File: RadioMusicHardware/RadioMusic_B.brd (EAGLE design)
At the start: 106 x 19.7 mm, 33 parts, among them IC1 TL072P, IC2 TL072P, IC3 7805L, U1 TEENSY_3.1_TW

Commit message: Back board reworking
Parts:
- removed IC1, IC2: TL072P, TomW:DIL08
- removed R6: (no value), bourns:3362P
- added IC4: TL074, linear:DIL14
- added OUTPUT: (no value), bourns:3362P
- D1, D2, D3, D4: value BAT81 -> (none)
- JP1: value M11LOCK -> M11PTH; device SparkFun-Connectors:1X11_LOCK -> SparkFun-Connectors:1X11
- JP3: device SparkFun-Connectors:1X07_LOCK -> SparkFun-Connectors:1X07
- moved C8 34.0 mm to (72.4, 9.53)
- moved JP1 22.9 mm to (82.5, 17.1), turned to 180 degrees
- moved IC3 20.1 mm to (26.0, 6.99), turned to 270 degrees
- moved C5 15.5 mm to (50.8, 8.76)
- moved R7 11.4 mm to (82.5, 8.89)
- moved D3 11.2 mm to (21.4, 8.31), turned to 270 degrees
- moved D4 11.0 mm to (19.1, 8.31), turned to 90 degrees
- moved C1 10.9 mm to (40.0, 1.27), turned to 0 degrees
- moved R2 10.2 mm to (17.1, 9.53)
- moved R5 8.47 mm to (49.5, 1.27), turned to 0 degrees
- moved C4 6.38 mm to (45.7, 8.89), turned to 270 degrees
- moved JP3 4.49 mm to (57.1, 1.27)
- moved C2 3.86 mm to (38.1, 8.89)
- moved C6 3.17 mm to (87.0, 6.35), turned to 180 degrees
- moved D2 2.84 mm to (8.89, 9.53), turned to 90 degrees
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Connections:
- new net N$3: IC4.6, IC4.7, R1.2
- net +12V: now also C5.2, IC4.4; no longer C5.1, IC1.8, IC2.8
- net -12V: now also C8.2, IC4.11; no longer C8.1, IC1.4, IC2.4
- net AUDIO_OUT: now also IC4.1, OUTPUT.2, OUTPUT.3; no longer IC2.1, R6.2, R6.3
- net CHANNEL_CV: now also IC4.5; no longer IC1.3
- net DGND: no longer C5.2, C8.2
- net GND: now also C5.1, C8.1, JP1.1, R7.2; no longer JP1.11, R7.1
- net LED1: now also JP1.2; no longer JP1.1
- net LED2: now also JP1.3; no longer JP1.2
- net LED3: now also JP1.4; no longer JP1.3
- net LED4: now also JP1.5; no longer JP1.4
- net LED_RESET: now also JP1.10; no longer JP1.9
- net MISO: now also JP1.11; no longer JP1.10
- net MOSI: now also JP1.6; no longer JP1.5
- net N$1: now also IC4.8, IC4.9, R2.2; no longer IC1.6, IC1.7, R2.1
- net N$10: now also R3.2; no longer R3.1
- net N$2: now also IC4.12, R4.2; no longer IC2.5, R4.1
- net N$4: now also R3.1, R4.1; no longer R3.2, R4.2
- net N$5: now also C3.1, IC4.13, IC4.14; no longer C3.2, IC2.6, IC2.7
- net N$6: now also C3.2, IC4.3; no longer C3.1, IC2.3
- net N$7: now also IC4.2, OUTPUT.1, R7.1; no longer IC2.2, R6.1, R7.2
- net PIN20/A6: now also R2.1; no longer R2.2
- net PIN22/A8: no longer IC1.1, IC1.2, R1.2
- net RESET_CV: now also JP1.8; no longer JP1.7
- net RESET_SW: now also JP1.7; no longer JP1.6
- net SS: now also JP1.9; no longer JP1.8
- net TIME_CV: now also IC4.10; no longer IC1.5
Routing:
- net +12V: track 0.00 -> 71.4 mm
- net LED1: track 0.00 -> 71.0 mm
- net LED2: track 0.00 -> 64.0 mm
- net LED3: track 0.00 -> 59.0 mm
- net LED4: track 0.00 -> 54.0 mm
- net N$1: track 0.00 -> 53.7 mm
- net MOSI: track 0.00 -> 48.8 mm
- net RESET_SW: track 0.00 -> 44.3 mm
- net RESET_CV: track 0.00 -> 38.6 mm
- net SS: track 0.00 -> 34.1 mm
- net -12V: track 0.00 -> 32.7 mm
- net +5V: track 0.00 -> 29.6 mm
- net LED_RESET: track 0.00 -> 28.7 mm
- net MISO: track 0.00 -> 22.2 mm
- net -12V_INLET: track 0.00 -> 17.7 mm
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- added copper zone on layer 16, net DGND
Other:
- board size 106 x 19.7 mm -> 107 x 19.5 mm

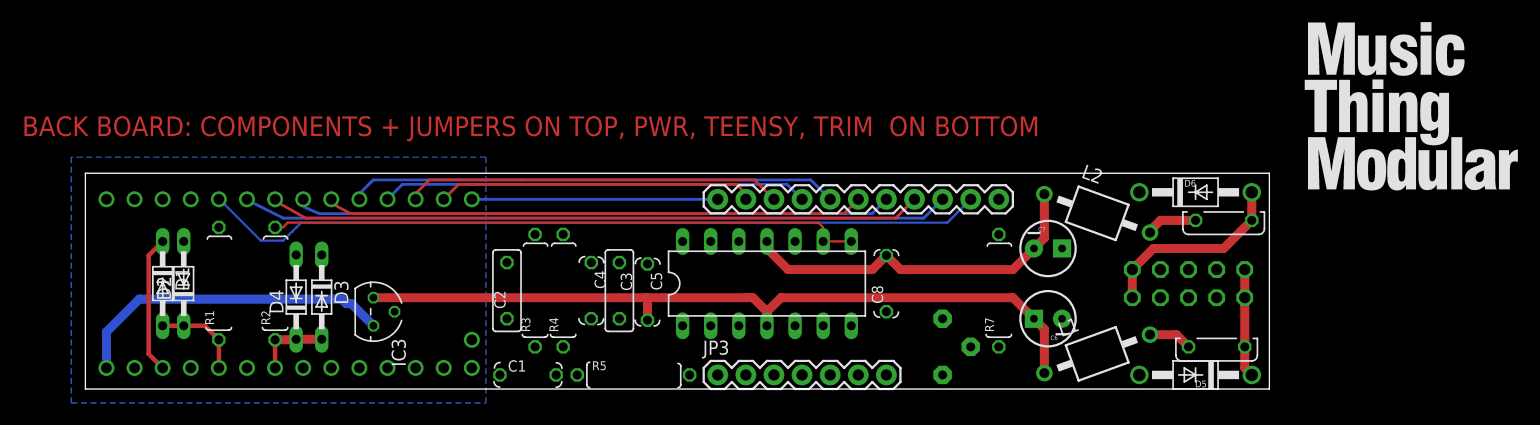
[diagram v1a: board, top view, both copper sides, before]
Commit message: Routed boards for checking
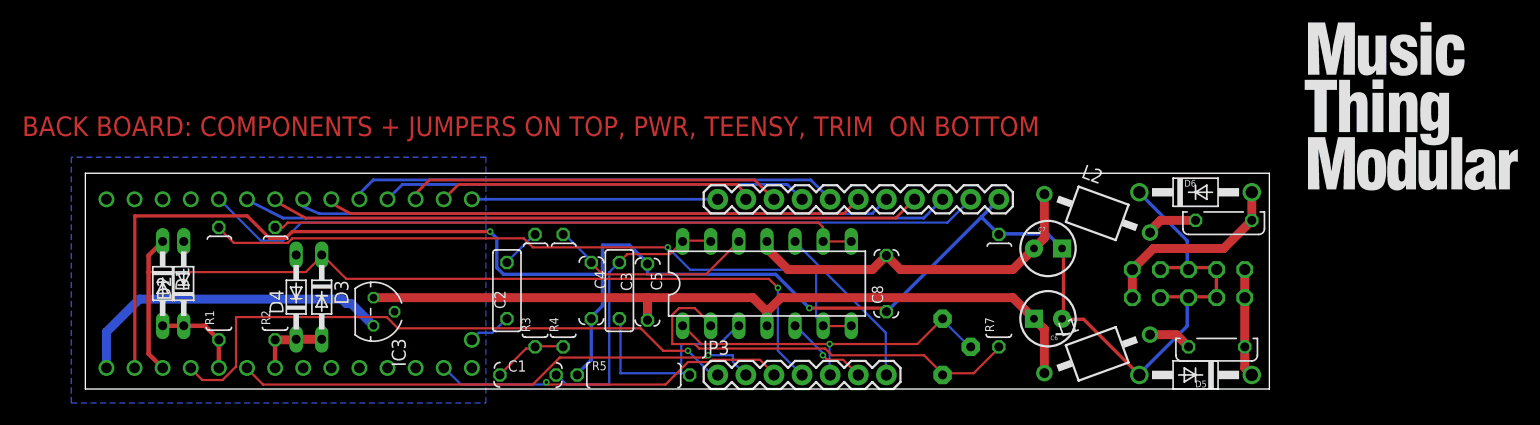
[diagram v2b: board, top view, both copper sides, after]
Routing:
- net GND: track 0.00 -> 170.9 mm, vias 0 -> 2
- net +3.3V: track 12.5 -> 80.0 mm, vias 0 -> 1
- net N$3: track 0.00 -> 63.8 mm, vias 0 -> 1
- net CHANNEL_POT: track 0.00 -> 55.3 mm, vias 0 -> 1
- net TIME_POT: track 0.00 -> 47.9 mm, vias 0 -> 1
- net N$7: track 0.00 -> 38.9 mm
- net SCLK: track 0.00 -> 32.3 mm, vias 0 -> 1
- net AUDIO_OUT: track 0.00 -> 31.6 mm, vias 0 -> 1
- net N$5: track 0.00 -> 25.7 mm
- net N$6: track 0.00 -> 19.8 mm
- net N$2: track 0.00 -> 18.8 mm
- net TIME_CV: track 0.00 -> 15.5 mm
- net CHANNEL_CV: track 0.00 -> 7.67 mm, vias 0 -> 1
- net N$4: track 0.00 -> 6.93 mm
- net DAC: track 0.00 -> 3.96 mm
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
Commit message: Artwork on panels, notes on PCBs
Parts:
- moved U$2 38.2 mm to (76.8, 0.15), flipped to the bottom, turned to 90 degrees
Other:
- board text added: "<-Set output volume"
- board text added: "Inspired by: John Cage Don Buchla Stockhausen Nicholas Collins Max Neuhaus, Akin Fernandez UbuWeb Resonance FM Thanks to: Paul Stoffregen, Steven Thonk The Muff Wigglers"
- board text added: "RadioMusic Back PCB Rev 1 Designed in Herne Hill, London by Tom Whitwell October 2014 CC-BY-SA musicthing.co.uk"
- board text added: "TEENSY 3.1"
- board text added: "USB this end"
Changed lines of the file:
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@@
 <grid distance="16" unitdist="mil" unit="mil" style="lines" multiple="1" display="yes" altdistance="8" altunitdist="mil" altunit="mil"/>
 <layers>
-<layer number="1" name="Top" color="4" fill="1" visible="yes" active="yes"/>
+<layer number="1" name="Top" color="4" fill="1" visible="no" active="yes"/>
 <layer number="2" name="Route2" color="1" fill="3" visible="no" active="yes"/>
 <layer number="3" name="Route3" color="4" fill="3" visible="no" active="no"/>
 <layer number="14" name="Route14" color="1" fill="6" visible="no" active="no"/>
 <layer number="15" name="Route15" color="4" fill="6" visible="no" active="yes"/>
-<layer number="16" name="Bottom" color="1" fill="1" visible="yes" active="yes"/>
+<layer number="16" name="Bottom" color="1" fill="1" visible="no" active="yes"/>
 <layer number="17" name="Pads" color="2" fill="1" visible="yes" active="yes"/>
 <layer number="18" name="Vias" color="2" fill="1" visible="yes" active="yes"/>
-<layer number="19" name="Unrouted" color="6" fill="1" visible="yes" active="yes"/>
+<layer number="19" name="Unrouted" color="6" fill="1" visible="no" active="yes"/>
 <layer number="20" name="Dimension" color="15" fill="1" visible="yes" active="yes"/>
 <layer number="21" name="tPlace" color="7" fill="1" visible="yes" active="yes"/>
@@
 <layer number="24" name="bOrigins" color="15" fill="1" visible="yes" active="yes"/>
 <layer number="25" name="tNames" color="7" fill="1" visible="no" active="yes"/>
-<layer number="26" name="bNames" color="7" fill="1" visible="no" active="yes"/>
+<layer number="26" name="bNames" color="7" fill="1" visible="yes" active="yes"/>
 <layer number="27" name="tValues" color="7" fill="1" visible="no" active="yes"/>
-<layer number="28" name="bValues" color="7" fill="1" visible="no" active="yes"/>
+<layer number="28" name="bValues" color="7" fill="1" visible="yes" active="yes"/>
 <layer number="29" name="tStop" color="7" fill="3" visible="no" active="yes"/>
 <layer number="30" name="bStop" color="7" fill="6" visible="no" active="yes"/>
@@
 </text>
 <wire x1="53.5" y1="-10" x2="53.5" y2="30" width="0.1" layer="51"/>
-<wire x1="53.5" y1="-10" x2="53.5" y2="30" width="0.1" layer="51"/>
+<text x="71.12" y="7.3152" size="0.762" layer="22" rot="MR0">RadioMusic Back PCB  Rev 1
+Designed in Herne Hill, London by Tom Whitwell
+October 2014 CC-BY-SA
+musicthing.co.uk</text>
+<text x="73.5584" y="3.2512" size="1.016" layer="22" rot="MR0">&lt;-Set output volume</text>
+<text x="23.5712" y="7.7216" size="2.286" layer="22" rot="MR0">TEENSY 3.1</text>
+<text x="3.2512" y="13.8176" size="1.016" layer="22" rot="SMR270">USB this end</text>
+<text x="35.7632" y="15.4432" size="0.508" layer="22" rot="MR0" align="top-left">Inspired by:
+John Cage
+Don Buchla
+Stockhausen
+Nicholas Collins
+Max Neuhaus,
+Akin Fernandez
+UbuWeb
+Resonance FM
+Thanks to:
+Paul Stoffregen,
+Steven Thonk
+The Muff Wigglers</text>
 </plain>
 <attributes>
@@
 <attribute name="VALUE" x="104.14" y="15.24" size="0.6096" layer="27" ratio="10" rot="R180"/>
 </element>
-<element name="U$2" library="TW_logos" package="MTM_2CM_SCREEN_200DPI" value="" x="110.49" y="18.034"/>
-<element name="U1" library="TomW" package="TEENSY_3.1_TW" value="TEENSY_3.1_TW" x="18.415" y="9.525" rot="MR270"/>
+<element name="U$2" library="TW_logos" package="MTM_2CM_SCREEN_200DPI" value="" x="76.7588" y="0.1524" rot="MR90"/>
+<element name="U1" library="TomW" package="TEENSY_3.1_TW" value="TEENSY_3.1_TW" x="18.415" y="9.525" smashed="yes" rot="MR270"/>
 <element name="IC3" library="gm-regulators" package="TO92" value="7805L" x="26.035" y="6.985" rot="R270"/>
 <element name="D1" library="diode" package="DO34-7" value="" x="6.985" y="9.525" rot="R270"/>
@@
 </element>
 <element name="OUTPUT" library="bourns" package="3362P" value="" x="77.47" y="3.81" smashed="yes" rot="MR90">
-<attribute name="NAME" x="81.407" y="0.508" size="1.27" layer="26" ratio="10" rot="MR90"/>
 <attribute name="VALUE" x="72.263" y="0.5334" size="1.27" layer="28" ratio="10" rot="MR90"/>
 </element>

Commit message: PCB cosmetic changes
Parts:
- added U$1: (no value), TW_logos:MTM_1CM
- added U$3: (no value), TW_logos:CC_1CM_SCREENPRINT
- D1, D2, D3, D4: value (none) -> BAT81
- U$2: device TW_logos:MTM_2CM_SCREEN_200DPI -> TW_logos:THONK_1CM_SCREENPRINT
- moved U$2 6.44 mm to (83.2, 0.64)
- moved D3 0.87 mm to (22.2, 8.26)
- moved D4 0.64 mm to (19.7, 8.26)
- moved D2 0.63 mm to (9.53, 9.53)
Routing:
- net PIN20/A6: track 6.78 -> 7.64 mm
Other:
- board text added: "<-NB REMEMBER TO INSTALL THIS PIN ON THE TEENSY (AUDIO OUT!)"
- board text added: "<-Set output volume here"
- board text added: "Header sockets THIS SIDE->"
- board text added: "Teensy sockets THIS SIDE->"
- board text removed: "<-Set output volume"

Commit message: Text subbing
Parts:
- moved U$2 46.4 mm to (36.8, 0.64)
- moved U$1 45.1 mm to (81.3, 0.00)
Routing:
- net GND: track 170.9 -> 122.2 mm
- added copper zone on layer 16, net GND
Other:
- board text added: "->"
- board text added: "Radio Music Back PCB Rev 1 Designed in Herne Hill, London by Tom Whitwell October 2014 CC-BY-SA musicthing.co.uk"
- board text removed: "BACK BOARD: COMPONENTS + JUMPERS ON TOP, PWR, TEENSY, TRIM ON BOTTOM"
- board text removed: "RadioMusic Back PCB Rev 1 Designed in Herne Hill, London by Tom Whitwell October 2014 CC-BY-SA musicthing.co.uk"

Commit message: Add value to trimmer
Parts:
- OUTPUT: value (none) -> 50k

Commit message: Fixed issues on Rev1 proto boards
Diodes changed to BAT42
LED resistors changed to 2k
Ground error on Front board fixed
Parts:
- D1, D2, D3, D4: value BAT81 -> BAT42
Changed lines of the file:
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@@
 <attribute name="VALUE" x="29.2354" y="10.16" size="1.27" layer="27" ratio="12" rot="R270"/>
 </element>
-<element name="D1" library="diode" package="DO34-7" value="BAT81" x="6.985" y="9.525" smashed="yes" rot="R270">
+<element name="D1" library="diode" package="DO34-7" value="BAT42" x="6.985" y="9.525" smashed="yes" rot="R270">
 <attribute name="VALUE" x="4.572" y="12.6746" size="1.27" layer="27" ratio="10" rot="R270"/>
 </element>
-<element name="D2" library="diode" package="DO34-7" value="BAT81" x="9.525" y="9.525" smashed="yes" rot="R90"/>
+<element name="D2" library="diode" package="DO34-7" value="BAT42" x="9.525" y="9.525" smashed="yes" rot="R90"/>
 <element name="R4" library="TomW" package="0207/10" value="8.2k" x="43.18" y="8.89" rot="R90"/>
 <element name="R3" library="TomW" package="0207/10" value="8.2k" x="40.64" y="8.89" rot="R90"/>
@@
 <element name="C2" library="TomW" package="C050-025X075" value="100n" x="38.1" y="8.89" rot="R90"/>
 <element name="R1" library="TomW" package="0207/10" value="47R" x="12.065" y="9.525" rot="R90"/>
-<element name="D3" library="diode" package="DO34-7" value="BAT81" x="22.225" y="8.255" smashed="yes" rot="R270"/>
-<element name="D4" library="diode" package="DO34-7" value="BAT81" x="19.685" y="8.255" smashed="yes" rot="R90">
+<element name="D3" library="diode" package="DO34-7" value="BAT42" x="22.225" y="8.255" smashed="yes" rot="R270"/>
+<element name="D4" library="diode" package="DO34-7" value="BAT42" x="19.685" y="8.255" smashed="yes" rot="R90">
 <attribute name="VALUE" x="24.5364" y="5.1054" size="1.27" layer="27" ratio="10" rot="R90"/>
 </element>

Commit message: Corrected power regulator label
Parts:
- IC3: value 7805L -> 78L05
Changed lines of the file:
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@@
 </element>
 <element name="U1" library="TomW" package="TEENSY_3.1_TW" value="TEENSY_3.1_TW" x="18.415" y="9.525" smashed="yes" rot="MR270"/>
-<element name="IC3" library="gm-regulators" package="TO92" value="7805L" x="26.035" y="6.985" smashed="yes" rot="R270">
+<element name="IC3" library="gm-regulators" package="TO92" value="78L05" x="26.035" y="6.985" smashed="yes" rot="R270">
 <attribute name="VALUE" x="29.2354" y="10.16" size="1.27" layer="27" ratio="12" rot="R270"/>
 </element>
